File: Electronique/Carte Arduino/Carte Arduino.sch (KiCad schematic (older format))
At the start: 19 parts

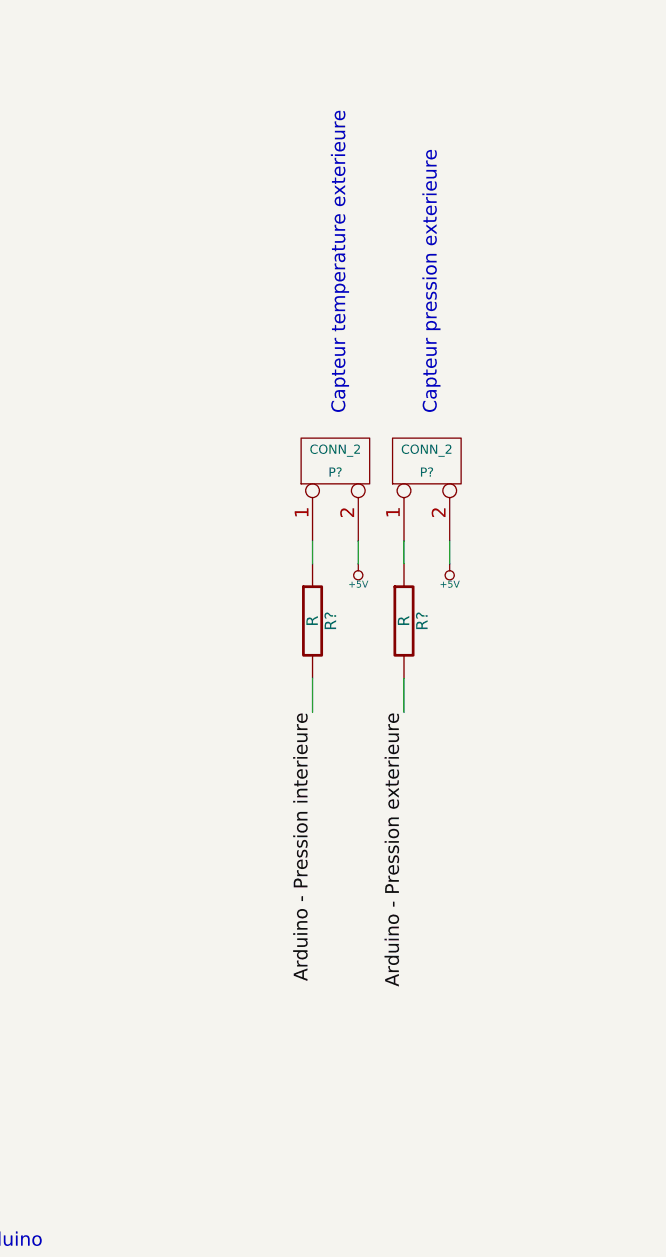
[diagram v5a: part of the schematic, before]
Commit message: Electronique/Carte Arduino/Carte Arduino.sch : - Implémentation des capteurs de pression
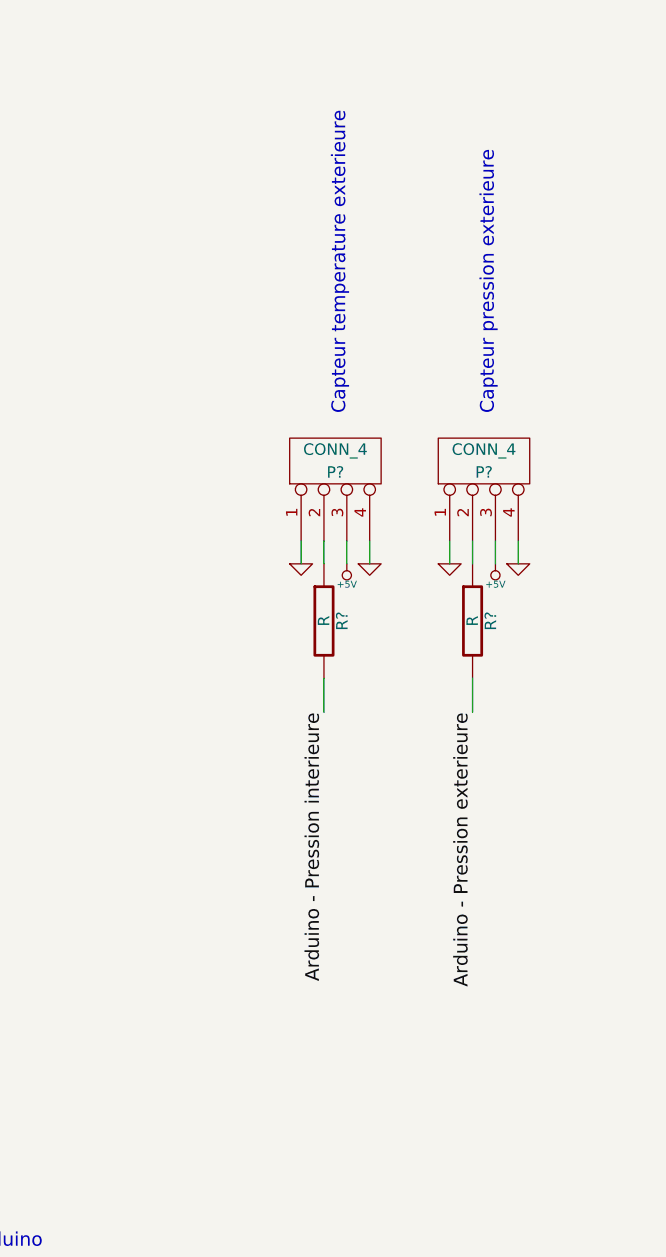
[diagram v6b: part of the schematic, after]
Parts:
- removed P? (x2): CONN_2, symbol CONN_2
- added P? (x2): CONN_4, symbol CONN_4
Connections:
- net +5V: now also P?.3 (P3), P?.3 (P3)
- net GND: now also P?.1 (P1), P?.1 (P1), P?.4 (P4), P?.4 (P4)
- net at R?.1: now also P?.2 (P2) (x2)
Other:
- moved on the sheet: R?
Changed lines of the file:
@@
-EESchema Schematic File Version 2  date 17/12/2011 22:59:16
+EESchema Schematic File Version 2  date 19/12/2011 13:42:36
 LIBS:power
 LIBS:device
@@
 Sheet 1 1
 Title ""
-Date "17 dec 2011"
+Date "19 dec 2011"
 Rev ""
 Comp ""
@@
 $Comp
 L GND #PWR?
+U 1 1 4EEF312B
+P 10000 2750
+F 0 "#PWR?" H 10000 2750 30  0001 C CNN
+F 1 "GND" H 10000 2680 30  0001 C CNN
+	1    10000 2750
+	1    0    0    -1
+$EndComp
+$Comp
+L GND #PWR?
+U 1 1 4EEF3129
+P 10300 2750
+F 0 "#PWR?" H 10300 2750 30  0001 C CNN
+F 1 "GND" H 10300 2680 30  0001 C CNN
+	1    10300 2750
+	1    0    0    -1
+$EndComp
+$Comp
+L GND #PWR?
+U 1 1 4EEF3125
+P 10650 2750
+F 0 "#PWR?" H 10650 2750 30  0001 C CNN
+F 1 "GND" H 10650 2680 30  0001 C CNN
+	1    10650 2750
+	1    0    0    -1
+$EndComp
+$Comp
+L GND #PWR?
+U 1 1 4EEF3122
+P 10950 2750
+F 0 "#PWR?" H 10950 2750 30  0001 C CNN
+F 1 "GND" H 10950 2680 30  0001 C CNN
+	1    10950 2750
+	1    0    0    -1
+$EndComp
+Wire Wire Line
+	10300 2650 10300 2750
+Wire Wire Line
+	10650 2650 10650 2750
+Connection ~ 1750 5300
+Wire Wire Line
+	1750 5300 1850 5300
+Connection ~ 1750 5250
+Wire Wire Line
+	1850 5250 1750 5250
+Wire Wire Line
+	1750 4750 1750 5350
+Wire Wire Line
+	950  5250 1050 5250
+Wire Wire Line
+	7850 5950 7750 5950
+Wire Wire Line
+	8400 2000 8400 2100
+Wire Wire Line
+	8200 2000 8200 2100
+Wire Wire Line
+	8000 2000 8000 2100
+Wire Wire Line
+	7800 2000 7800 2100
+Wire Wire Line
+	7850 6650 7750 6650
+Wire Wire Line
+	5300 2800 5300 2950
+Wire Wire Line
+	4250 2800 4250 2950
+Wire Wire Line
+	5500 2200 5500 2300
+Wire Wire Line
+	5300 2200 5300 2300
+Wire Wire Line
+	5100 2200 5100 2300
+Wire Wire Line
+	4450 2200 4450 2300
+Wire Wire Line
+	4250 2200 4250 2300
+Wire Wire Line
+	4050 2200 4050 2300
+Wire Wire Line
+	7750 6550 7850 6550
+Wire Wire Line
+	9550 6350 9650 6350
+Wire Wire Line
+	9550 6450 9650 6450
+Wire Wire Line
+	5950 6400 5950 6500
+Wire Wire Line
+	5750 6400 5750 6500
+Wire Wire Line
+	5550 6400 5550 6500
+Wire Wire Line
+	5150 6400 5150 6500
+Wire Wire Line
+	4950 6400 4950 6500
+Wire Wire Line
+	4750 6400 4750 6500
+Wire Wire Line
+	4550 6400 4550 6500
+Wire Wire Line
+	4150 6400 4150 6500
+Wire Wire Line
+	3950 6400 3950 6500
+Wire Wire Line
+	10750 3250 10750 3400
+Wire Wire Line
+	10750 2650 10750 2750
+Wire Wire Line
+	10850 2750 10850 2650
+Wire Wire Line
+	10200 2750 10200 2650
+Wire Wire Line
+	10100 2650 10100 2750
+Wire Wire Line
+	10100 3250 10100 3400
+Wire Wire Line
+	1750 5850 1750 6000
+Wire Wire Line
+	1950 4850 1950 4750
+Wire Wire Line
+	1150 4850 1150 4750
+Wire Wire Line
+	950  5850 950  6000
+Wire Wire Line
+	3850 6400 3850 6500
+Wire Wire Line
+	4050 6400 4050 6500
+Wire Wire Line
+	4450 6400 4450 6500
+Wire Wire Line
+	4650 6400 4650 6500
+Wire Wire Line
+	4850 6400 4850 6500
+Wire Wire Line
+	5050 6400 5050 6500
+Wire Wire Line
+	5450 6400 5450 6500
+Wire Wire Line
+	5650 6400 5650 6500
+Wire Wire Line
+	5850 6400 5850 6500
+Wire Wire Line
+	6050 6400 6050 6500
+Wire Wire Line
+	6150 6400 6150 6500
+Wire Wire Line
+	9550 6500 9650 6500
+Wire Wire Line
+	9550 6400 9650 6400
+Wire Wire Line
+	7850 6500 7750 6500
+Wire Wire Line
+	3950 2200 3950 2300
+Wire Wire Line
+	4150 2200 4150 2300
+Wire Wire Line
+	4350 2200 4350 2300
+Wire Wire Line
+	5000 2200 5000 2300
+Wire Wire Line
+	5200 2200 5200 2300
+Wire Wire Line
+	5400 2200 5400 2300
+Wire Wire Line
+	7850 6600 7750 6600
+Wire Wire Line
+	7700 2000 7700 2100
+Wire Wire Line
+	7900 2000 7900 2100
+Wire Wire Line
+	8100 2000 8100 2100
+Wire Wire Line
+	8300 2000 8300 2100
+Wire Wire Line
+	7850 5900 7750 5900
+Wire Wire Line
+	1150 4750 1050 4750
+Wire Wire Line
+	950  4750 950  5350
+Connection ~ 950  5250
+Wire Wire Line
+	1950 4750 1850 4750
+Wire Wire Line
+	950  5300 850  5300
+Connection ~ 950  5300
+Wire Wire Line
+	10950 2650 10950 2750
+Wire Wire Line
+	10000 2650 10000 2750
+$Comp
+L CONN_4 P?
+U 1 1 4EEF306B
+P 10800 2300
+F 0 "P?" V 10750 2300 50  0000 C CNN
+F 1 "CONN_4" V 10850 2300 50  0000 C CNN
+	1    10800 2300
+	0    -1   -1   0
+$EndComp
+$Comp
+L CONN_4 P?
+U 1 1 4EEF305D
+P 10150 2300
+F 0 "P?" V 10100 2300 50  0000 C CNN
+F 1 "CONN_4" V 10200 2300 50  0000 C CNN
+	1    10150 2300
+	0    -1   -1   0
+$EndComp
+$Comp
+L GND #PWR?
 U 1 1 4EED108C
 P 1750 6000
@@
 	1    0    0    -1
 $EndComp
-Connection ~ 1750 5300
-Wire Wire Line
-	1750 5300 1850 5300
-Connection ~ 1750 5250
-Wire Wire Line
-	1850 5250 1750 5250
-Wire Wire Line
-	1750 4750 1750 5350
-Wire Wire Line
-	950  5250 1050 5250
-Wire Wire Line
-	7850 5950 7750 5950
-Wire Wire Line
-	8400 2000 8400 2100
-Wire Wire Line
-	8200 2000 8200 2100
-Wire Wire Line
-	8000 2000 8000 2100
-Wire Wire Line
-	7800 2000 7800 2100
-Wire Wire Line
-	7850 6650 7750 6650
-Wire Wire Line
-	5300 2800 5300 2950
-Wire Wire Line
-	4250 2800 4250 2950
-Wire Wire Line
-	5500 2200 5500 2300
-Wire Wire Line
-	5300 2200 5300 2300
-Wire Wire Line
-	5100 2200 5100 2300
-Wire Wire Line
-	4450 2200 4450 2300
-Wire Wire Line
-	4250 2200 4250 2300
-Wire Wire Line
-	4050 2200 4050 2300
-Wire Wire Line
-	7750 6550 7850 6550
-Wire Wire Line
-	9550 6350 9650 6350
-Wire Wire Line
-	9550 6450 9650 6450
-Wire Wire Line
-	5950 6400 5950 6500
-Wire Wire Line
-	5750 6400 5750 6500
-Wire Wire Line
-	5550 6400 5550 6500
-Wire Wire Line
-	5150 6400 5150 6500
-Wire Wire Line
-	4950 6400 4950 6500
-Wire Wire Line
-	4750 6400 4750 6500
-Wire Wire Line
-	4550 6400 4550 6500
-Wire Wire Line
-	4150 6400 4150 6500
-Wire Wire Line
-	3950 6400 3950 6500
-Wire Wire Line
-	10450 3250 10450 3400
-Wire Wire Line
-	10450 2650 10450 2750
-Wire Wire Line
-	10650 2750 10650 2650
-Wire Wire Line
-	10250 2750 10250 2650
-Wire Wire Line
-	10050 2650 10050 2750
-Wire Wire Line
-	10050 3250 10050 3400
-Wire Wire Line
-	1750 5850 1750 6000
-Wire Wire Line
-	1950 4850 1950 4750
-Wire Wire Line
-	1150 4850 1150 4750
-Wire Wire Line
-	950  5850 950  6000
-Wire Wire Line
-	3850 6400 3850 6500
-Wire Wire Line
-	4050 6400 4050 6500
-Wire Wire Line
-	4450 6400 4450 6500
-Wire Wire Line
-	4650 6400 4650 6500
-Wire Wire Line
-	4850 6400 4850 6500
-Wire Wire Line
-	5050 6400 5050 6500
-Wire Wire Line
-	5450 6400 5450 6500
-Wire Wire Line
-	5650 6400 5650 6500
-Wire Wire Line
-	5850 6400 5850 6500
-Wire Wire Line
-	6050 6400 6050 6500
-Wire Wire Line
-	6150 6400 6150 6500
-Wire Wire Line
-	9550 6500 9650 6500
-Wire Wire Line
-	9550 6400 9650 6400
-Wire Wire Line
-	7850 6500 7750 6500
-Wire Wire Line
-	3950 2200 3950 2300
-Wire Wire Line
-	4150 2200 4150 2300
-Wire Wire Line
-	4350 2200 4350 2300
-Wire Wire Line
-	5000 2200 5000 2300
-Wire Wire Line
-	5200 2200 5200 2300
-Wire Wire Line
-	5400 2200 5400 2300
-Wire Wire Line
-	7850 6600 7750 6600
-Wire Wire Line
-	7700 2000 7700 2100
-Wire Wire Line
-	7900 2000 7900 2100
-Wire Wire Line
-	8100 2000 8100 2100
-Wire Wire Line
-	8300 2000 8300 2100
-Wire Wire Line
-	7850 5900 7750 5900
-Wire Wire Line
-	1150 4750 1050 4750
-Wire Wire Line
-	950  4750 950  5350
-Connection ~ 950  5250
-Wire Wire Line
-	1950 4750 1850 4750
-Wire Wire Line
-	950  5300 850  5300
-Connection ~ 950  5300
 $Comp
 L R R?
@@
 Text Notes 10200 2100 1    60   ~ 0
 Capteur temperature exterieure
-Text Notes 10600 2100 1    60   ~ 0
+Text Notes 10850 2100 1    60   ~ 0
 Capteur pression exterieure
 Text Notes 1900 4200 1    60   ~ 0
@@
 L +5V #PWR05
 U 1 1 4EE364FB
-P 10650 2750
-F 0 "#PWR05" H 10650 2840 20  0001 C CNN
-F 1 "+5V" H 10650 2840 30  0000 C CNN
-	1    10650 2750
-	-1   0    0    1
-$EndComp
-$Comp
-L CONN_2 P?
-U 1 1 4EE364FA
-P 10550 2300
-F 0 "P?" V 10500 2300 40  0000 C CNN
-F 1 "CONN_2" V 10600 2300 40  0000 C CNN
-	1    10550 2300
-	0    -1   -1   0
-$EndComp
-Text Label 10450 3400 3    60   ~ 0
+P 10850 2750
+F 0 "#PWR05" H 10850 2840 20  0001 C CNN
+F 1 "+5V" H 10850 2840 30  0000 C CNN
+	1    10850 2750
+	-1   0    0    1
+$EndComp
+Text Label 10750 3400 3    60   ~ 0
 Arduino - Pression exterieure
 $Comp
 L R R?
 U 1 1 4EE364F9
-P 10450 3000
-F 0 "R?" V 10530 3000 50  0000 C CNN
-F 1 "R" V 10450 3000 50  0000 C CNN
-	1    10450 3000
+P 10750 3000
+F 0 "R?" V 10830 3000 50  0000 C CNN
+F 1 "R" V 10750 3000 50  0000 C CNN
+	1    10750 3000
 	1    0    0    -1
 $EndComp
@@
 L R R?
 U 1 1 4EE364F8
-P 10050 3000
-F 0 "R?" V 10130 3000 50  0000 C CNN
-F 1 "R" V 10050 3000 50  0000 C CNN
-	1    10050 3000
-	1    0    0    -1
-$EndComp
-Text Label 10050 3400 3    60   ~ 0
+P 10100 3000
+F 0 "R?" V 10180 3000 50  0000 C CNN
+F 1 "R" V 10100 3000 50  0000 C CNN
+	1    10100 3000
+	1    0    0    -1
+$EndComp
+Text Label 10100 3400 3    60   ~ 0
 Arduino - Pression interieure
-$Comp
-L CONN_2 P?
-U 1 1 4EE364F7
-P 10150 2300
-F 0 "P?" V 10100 2300 40  0000 C CNN
-F 1 "CONN_2" V 10200 2300 40  0000 C CNN
-	1    10150 2300
-	0    -1   -1   0
-$EndComp
 $Comp
 L +5V #PWR06
 U 1 1 4EE364F6
-P 10250 2750
-F 0 "#PWR06" H 10250 2840 20  0001 C CNN
-F 1 "+5V" H 10250 2840 30  0000 C CNN
-	1    10250 2750
-	-1   0    0    1
-$EndComp
+P 10200 2750
+F 0 "#PWR06" H 10200 2840 20  0001 C CNN
+F 1 "+5V" H 10200 2840 30  0000 C CNN
+	1    10200 2750
+	-1   0    0    1
+$EndComp
